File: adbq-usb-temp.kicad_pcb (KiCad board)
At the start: 4 copper layers, 40.3 x 16 mm, 81 parts, among them J4 USB_C_Receptacle_USB2.0_14P, Q1 Q_NMOS, Q2 Q_NMOS, Q3 Q_NMOS, SW1 SW_Push, SW2 TestPoint, SW3 TestPoint, SW4 TestPoint, U1 ESP32-S3FH4R2, U14 TMP117AIDRV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

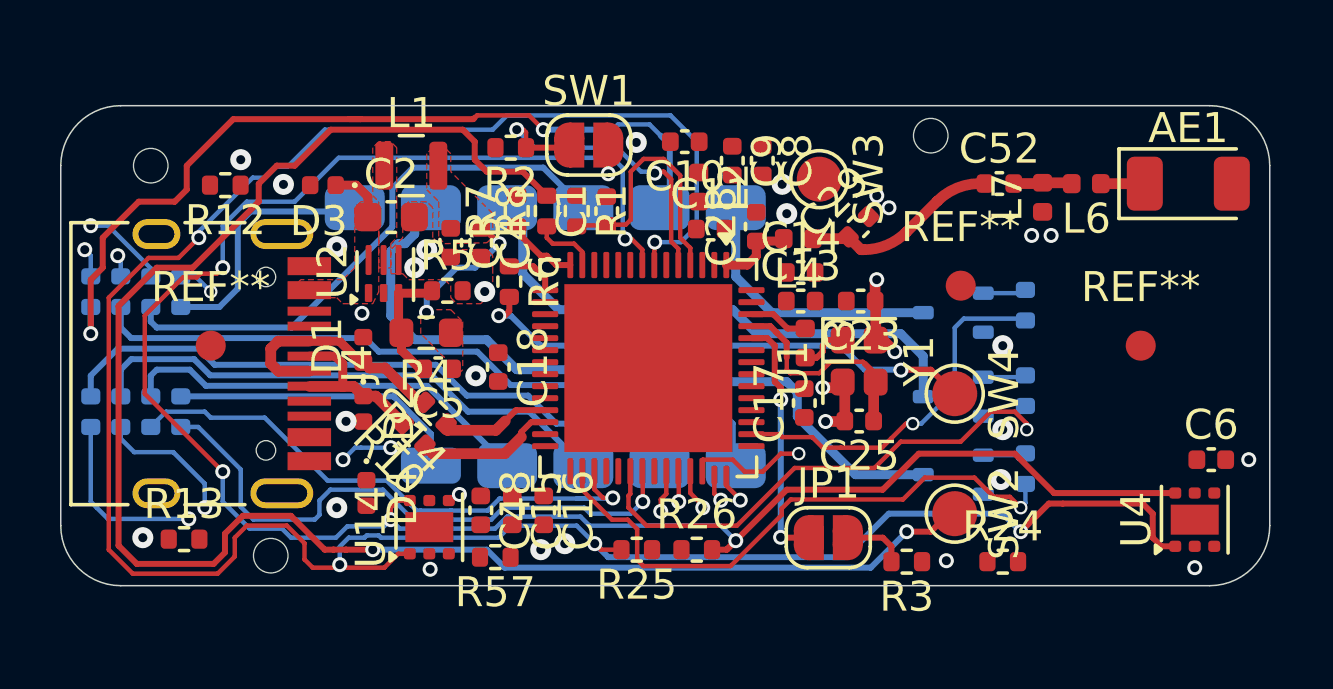
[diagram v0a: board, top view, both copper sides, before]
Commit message: pcb: add TMP117 routing
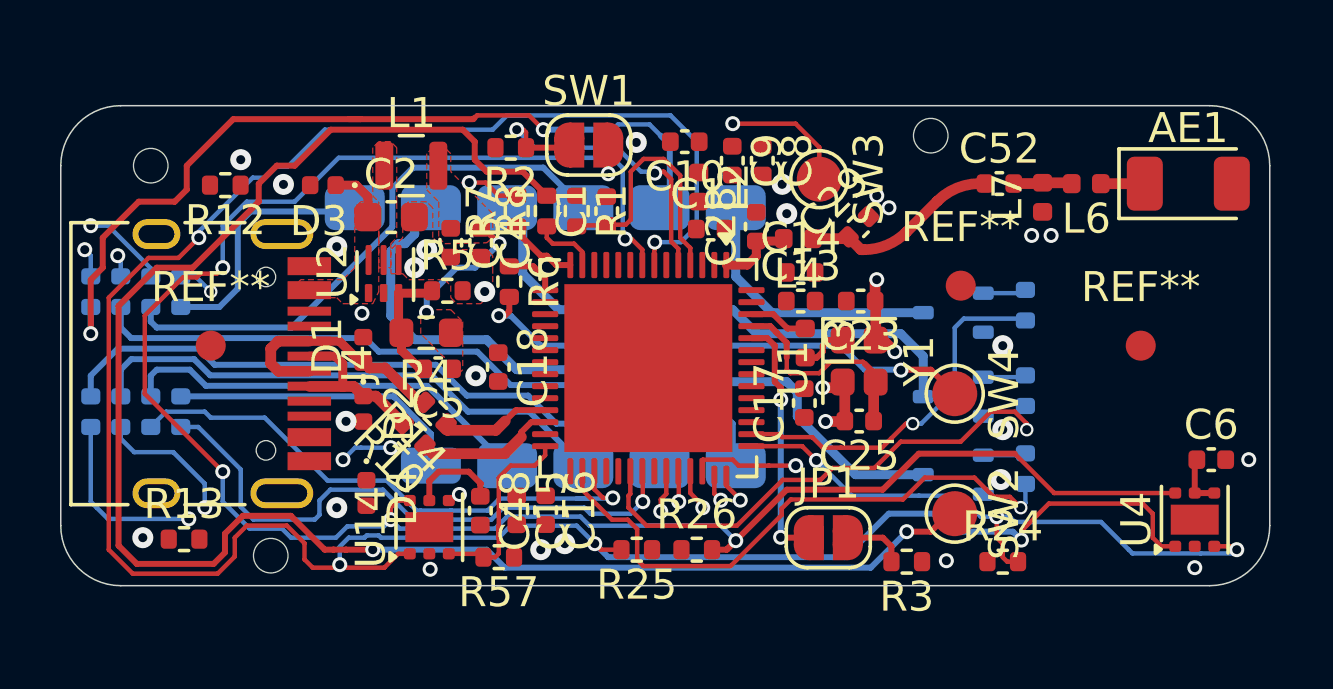
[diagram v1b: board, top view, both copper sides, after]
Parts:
- moved C15 0.15 mm to (97.2, 100.5)
- moved R57 0.11 mm to (96.6, 102.0)
- moved C16 0.06 mm to (98.2, 100.5)
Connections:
- U1 pad 23: /TMP117_ALERT_2 -> unconnected-(U1-GPIO17/ADC2_CH6-Pad23)
- U1 pad 24: /TMP117_ALERT -> unconnected-(U1-GPIO18/ADC2_CH7-Pad24)
- U1 pad 28: unconnected-(U1-SPI_CS1/GPIO26-Pad28) -> /TMP117_ALERT
- U1 pad 43: unconnected-(U1-GPIO38-Pad43) -> /TMP117_ALERT_2
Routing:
- net /TMP117_ALERT_2: track 0.00 -> 20.5 mm, vias 0 -> 3
- net Net-(R7-Pad2): track 0.00 -> 15.6 mm, vias 0 -> 2
- net /TMP117_ALERT: track 0.00 -> 6.74 mm
- net +3V3: track 4.52 -> 9.39 mm

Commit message: pcb: finish USB routing
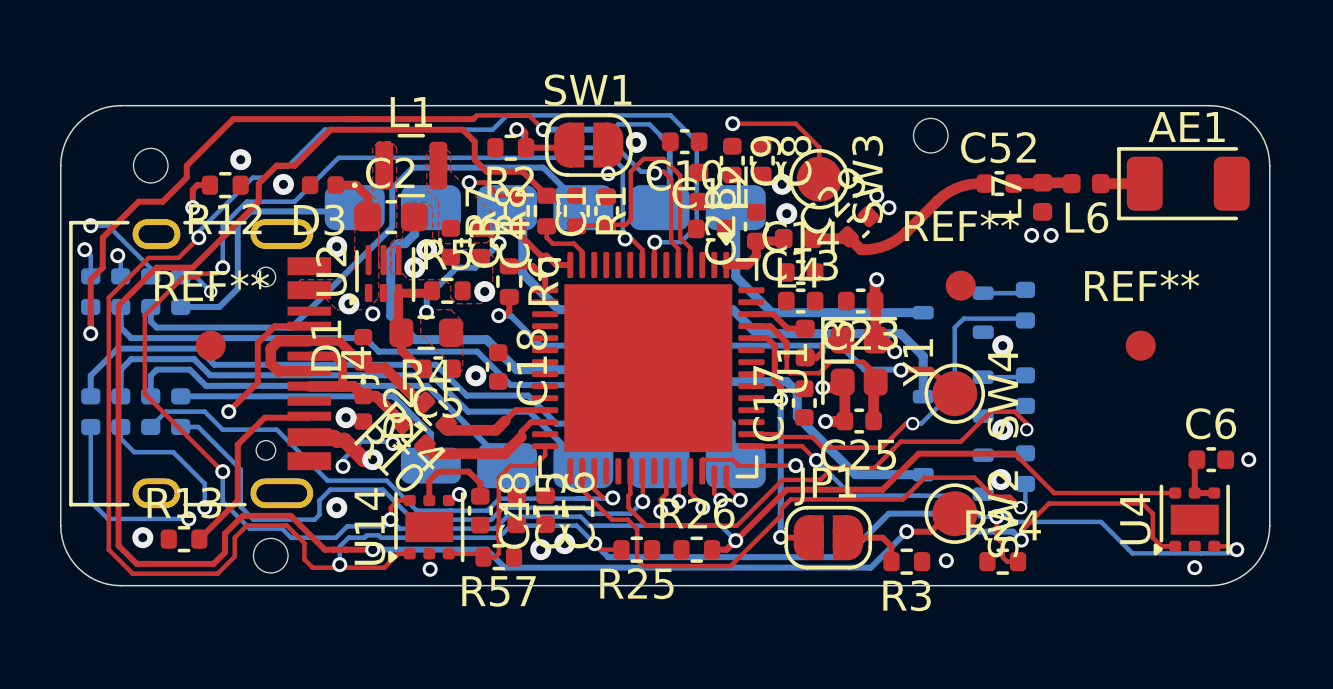
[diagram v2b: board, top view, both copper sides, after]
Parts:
- removed D4: H5VU10U, Pers:Diode_DFN1006
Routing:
- net Net-(J4-CC1): track 0.00 -> 13.5 mm, vias 0 -> 2
- net +5V: track 1.91 -> 9.86 mm, vias 0 -> 2
- net Net-(J4-CC2): track 0.00 -> 6.46 mm

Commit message: pcb: add 3v3 routing
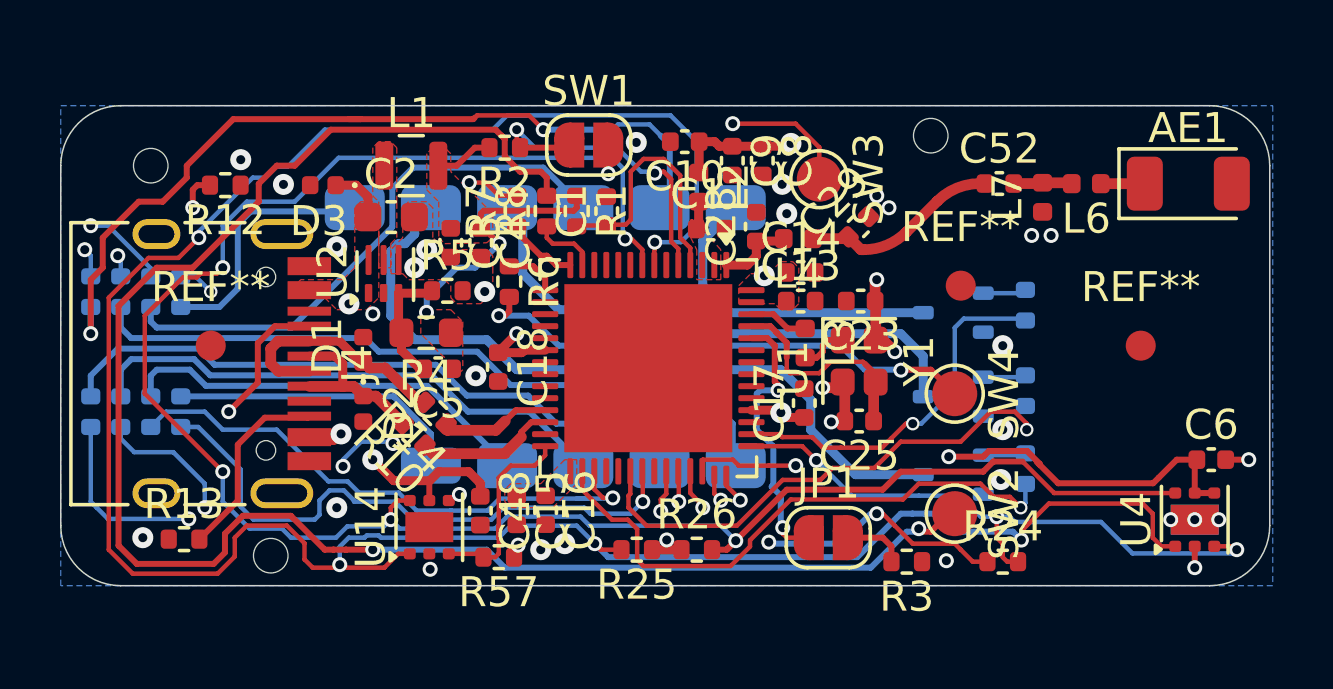
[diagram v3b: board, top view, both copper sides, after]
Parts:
- moved R2 0.20 mm to (96.8, 88.4)
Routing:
- net +3V3: track 9.39 -> 99.3 mm, vias 2 -> 12
- net GND: track 5.82 -> 20.2 mm
- net +5V: track 9.86 -> 7.46 mm
- net Net-(Q1-D): track 9.05 -> 10.8 mm
- net Net-(JP1-A): track 8.31 -> 9.30 mm
- net VDD3P3: track 0.00 -> 0.95 mm
- net (no net): vias 0 -> 2
- added copper zone on F.Cu, net /VDD_SPI
- added copper zone on B.Cu, net GND
- added copper zone on F.Cu, net VDD3P3

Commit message: pcb: add edge TMP117 pad and keepout
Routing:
- net GND: vias 33 -> 31
- net (no net): vias 2 -> 3
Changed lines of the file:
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@@
 			)
 		)
-		(pad "" smd roundrect
-			(at 0 -0.4 90)
-			(size 0.81 0.64)
-			(layers "F.Paste")
-			(roundrect_rratio 0.25)
-		)
-		(pad "" smd roundrect
-			(at 0 0.4 90)
-			(size 0.81 0.64)
-			(layers "F.Paste")
-			(roundrect_rratio 0.25)
-		)
 		(pad "1" smd roundrect
 			(at -0.8875 -0.65 90)
@@
 			)
 		)
-		(pad "" smd roundrect
-			(at 0 -0.4 90)
-			(size 0.81 0.64)
-			(layers "F.Paste")
-			(roundrect_rratio 0.25)
-		)
-		(pad "" smd roundrect
-			(at 0 0.4 90)
-			(size 0.81 0.64)
-			(layers "F.Paste")
-			(roundrect_rratio 0.25)
-		)
 		(pad "1" smd roundrect
 			(at -0.8875 -0.65 90)
@@
 			(size 1 1.6)
 			(property pad_prop_heatsink)
-			(layers "F.Mask" "B.Cu")
+			(layers "B.Cu" "B.Mask")
 			(zone_connect 2)
 		)
@@
 	)
 	(via
-		(at 119 100.8)
+		(at 119.2 100.8)
+		(size 0.5)
+		(drill 0.3)
+		(layers "F.Cu" "B.Cu")
+		(net 0)
+	)
+	(via
+		(at 120.4 100.8)
 		(size 0.5)
 		(drill 0.3)
@@
 	)
 	(via
-		(at 115.012527 91.326119)
-		(size 0.5)
-		(drill 0.3)
-		(layers "F.Cu" "B.Cu")
-		(net 3)
-	)
-	(via
 		(at 109.2 90)
 		(size 0.5)
@@
 	)
 	(via
-		(at 114.363912 91.326119)
-		(size 0.5)
-		(drill 0.3)
-		(layers "F.Cu" "B.Cu")
-		(net 3)
-	)
-	(via
 		(at 100.25183 89.269394)
 		(size 0.5)
@@
 	)
 	(via
-		(at 120.6 100.8)
-		(size 0.5)
+		(at 114.746222 91.214459)
+		(size 0.7)
 		(drill 0.3)
 		(layers "F.Cu" "B.Cu")
@@
 		(polygon
 			(pts
-				(xy 122.3575 87.35) (xy 122.3575 97.85) (xy 115.1075 97.85) (xy 115.1075 87.35)
+				(xy 122.4 87) (xy 122.4 103) (xy 111 103) (xy 111 93.5) (xy 115.6075 91.5) (xy 115.6075 87)
 			)
 		)

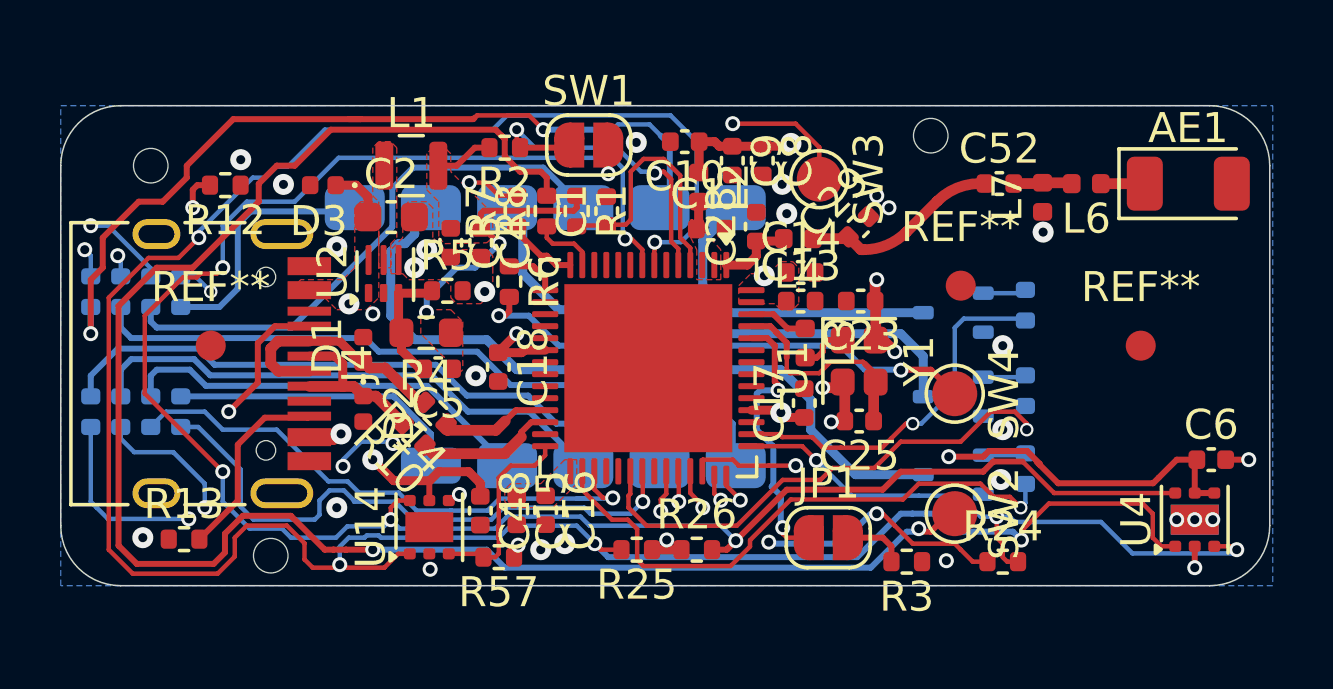
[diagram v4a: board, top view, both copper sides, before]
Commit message: pcb: add TMP117 board cutout
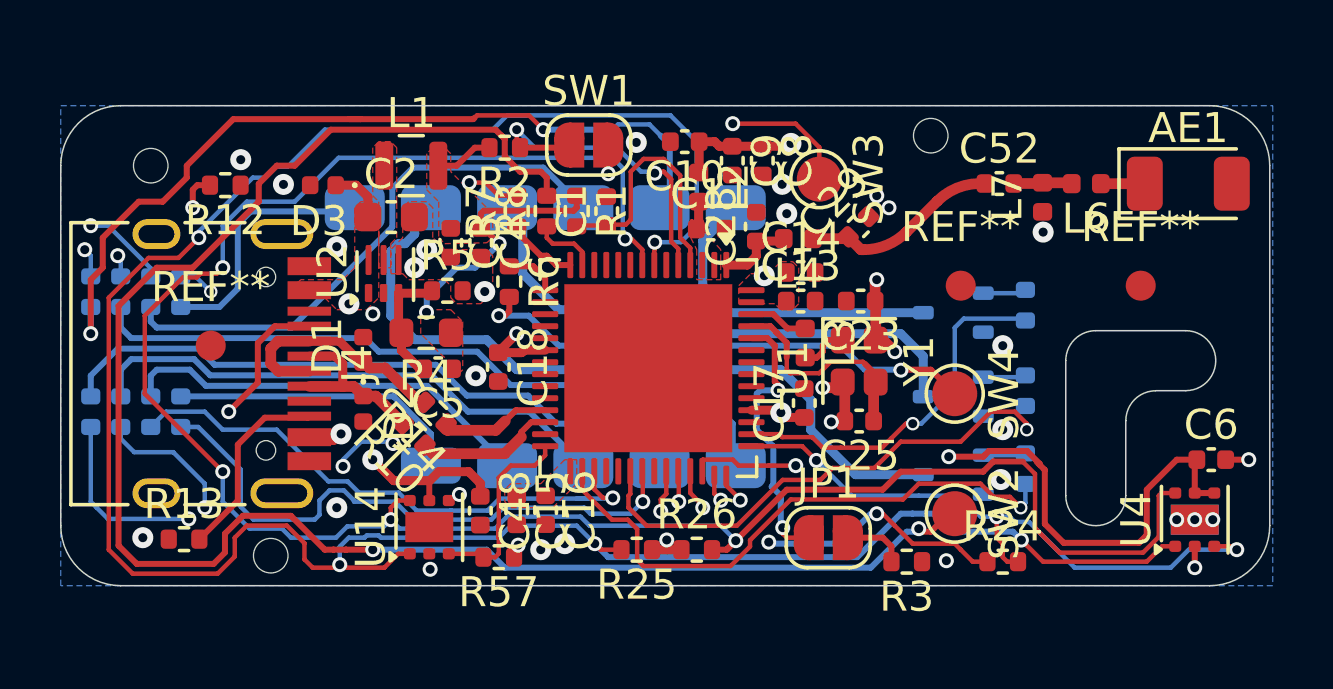
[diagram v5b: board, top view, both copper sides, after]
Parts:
- moved REF** 2.00 mm to (118.0, 93.0)
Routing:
- net +3V3: track 99.3 -> 102.8 mm
- net /SDA: track 67.1 -> 70.6 mm
- net /SCL: track 81.8 -> 80.6 mm
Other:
- outline, holes or cut-outs redrawn

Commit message: pcb: add top GND pour
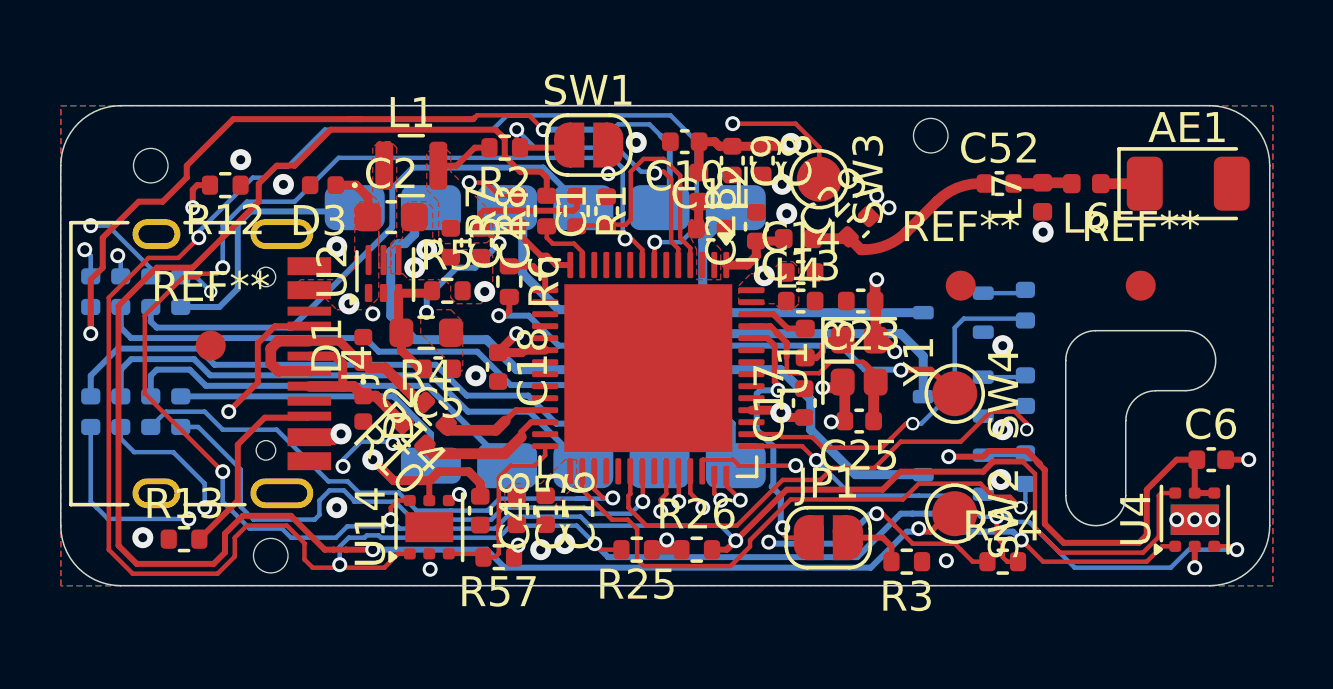
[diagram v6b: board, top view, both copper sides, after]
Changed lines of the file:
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@@
+	)
+	(zone
+		(net 3)
+		(net_name "GND")
+		(layers "F.Cu" "B.Cu")
+		(hatch edge 0.5)
+		(connect_pads
+			(clearance 0.2)
+		)
+		(min_thickness 0.15)
+		(filled_areas_thickness no)
+		(fill yes
+			(thermal_gap 0.4)
+			(thermal_bridge_width 0.25)
+		)
+		(polygon
+			(pts
+				(xy 82 87) (xy 122.4 87) (xy 122.4 103) (xy 82 103)
+			)
+		)
 	)
 	(zone
@@
 			)
 		)
-	)
-	(zone
-		(net 3)
-		(net_name "GND")
-		(layer "B.Cu")
-		(hatch edge 0.5)
-		(connect_pads
-			(clearance 0.2)
-		)
-		(min_thickness 0.15)
-		(filled_areas_thickness no)
-		(fill yes
-			(thermal_gap 0.4)
-			(thermal_bridge_width 0.25)
-		)
-		(polygon
-			(pts
-				(xy 82 87) (xy 122.4 87) (xy 122.4 103) (xy 82 103)
-			)
-		)

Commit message: pcb: add stitching vias
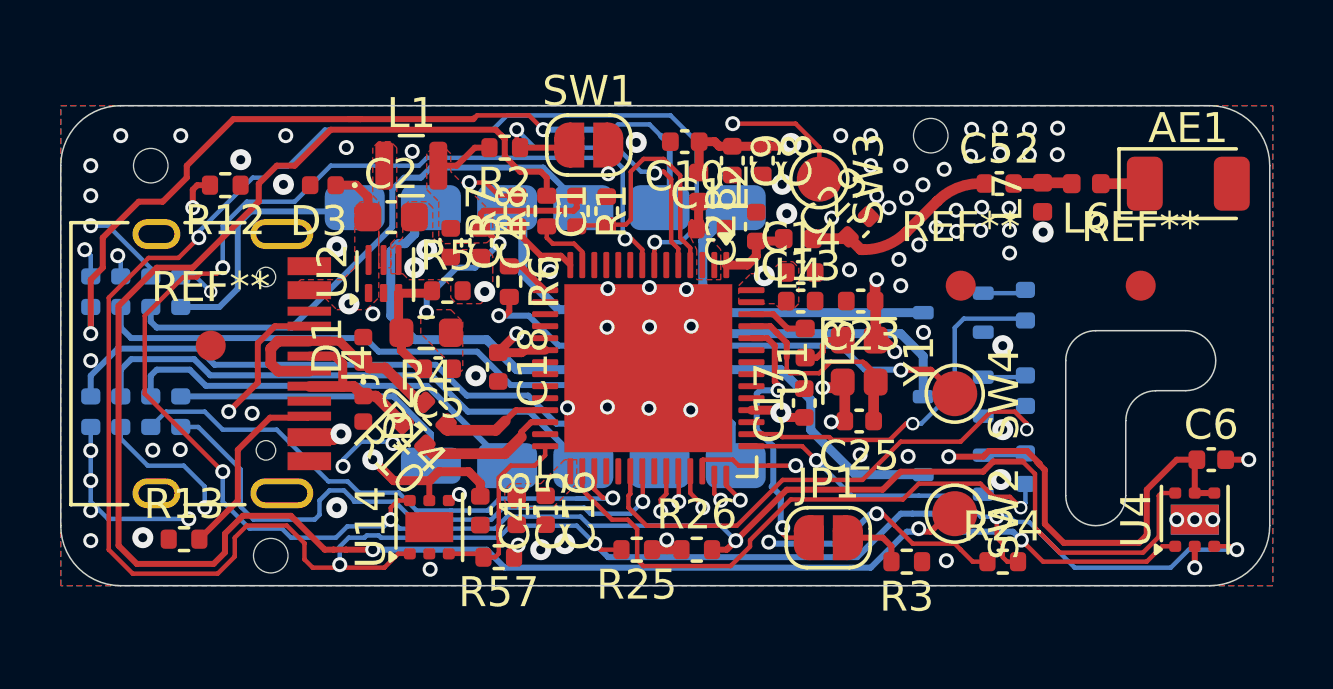
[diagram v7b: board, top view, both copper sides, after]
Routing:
- net GND: vias 31 -> 88

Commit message: pcb: clean tracks
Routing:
- net Net-(J4-CC1): track 13.5 -> 12.8 mm
- net +3V3: track 102.8 -> 102.2 mm
- net Net-(U3-A): track 28.3 -> 27.8 mm
- net GND: vias 88 -> 95
